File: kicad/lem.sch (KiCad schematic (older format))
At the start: 56 parts

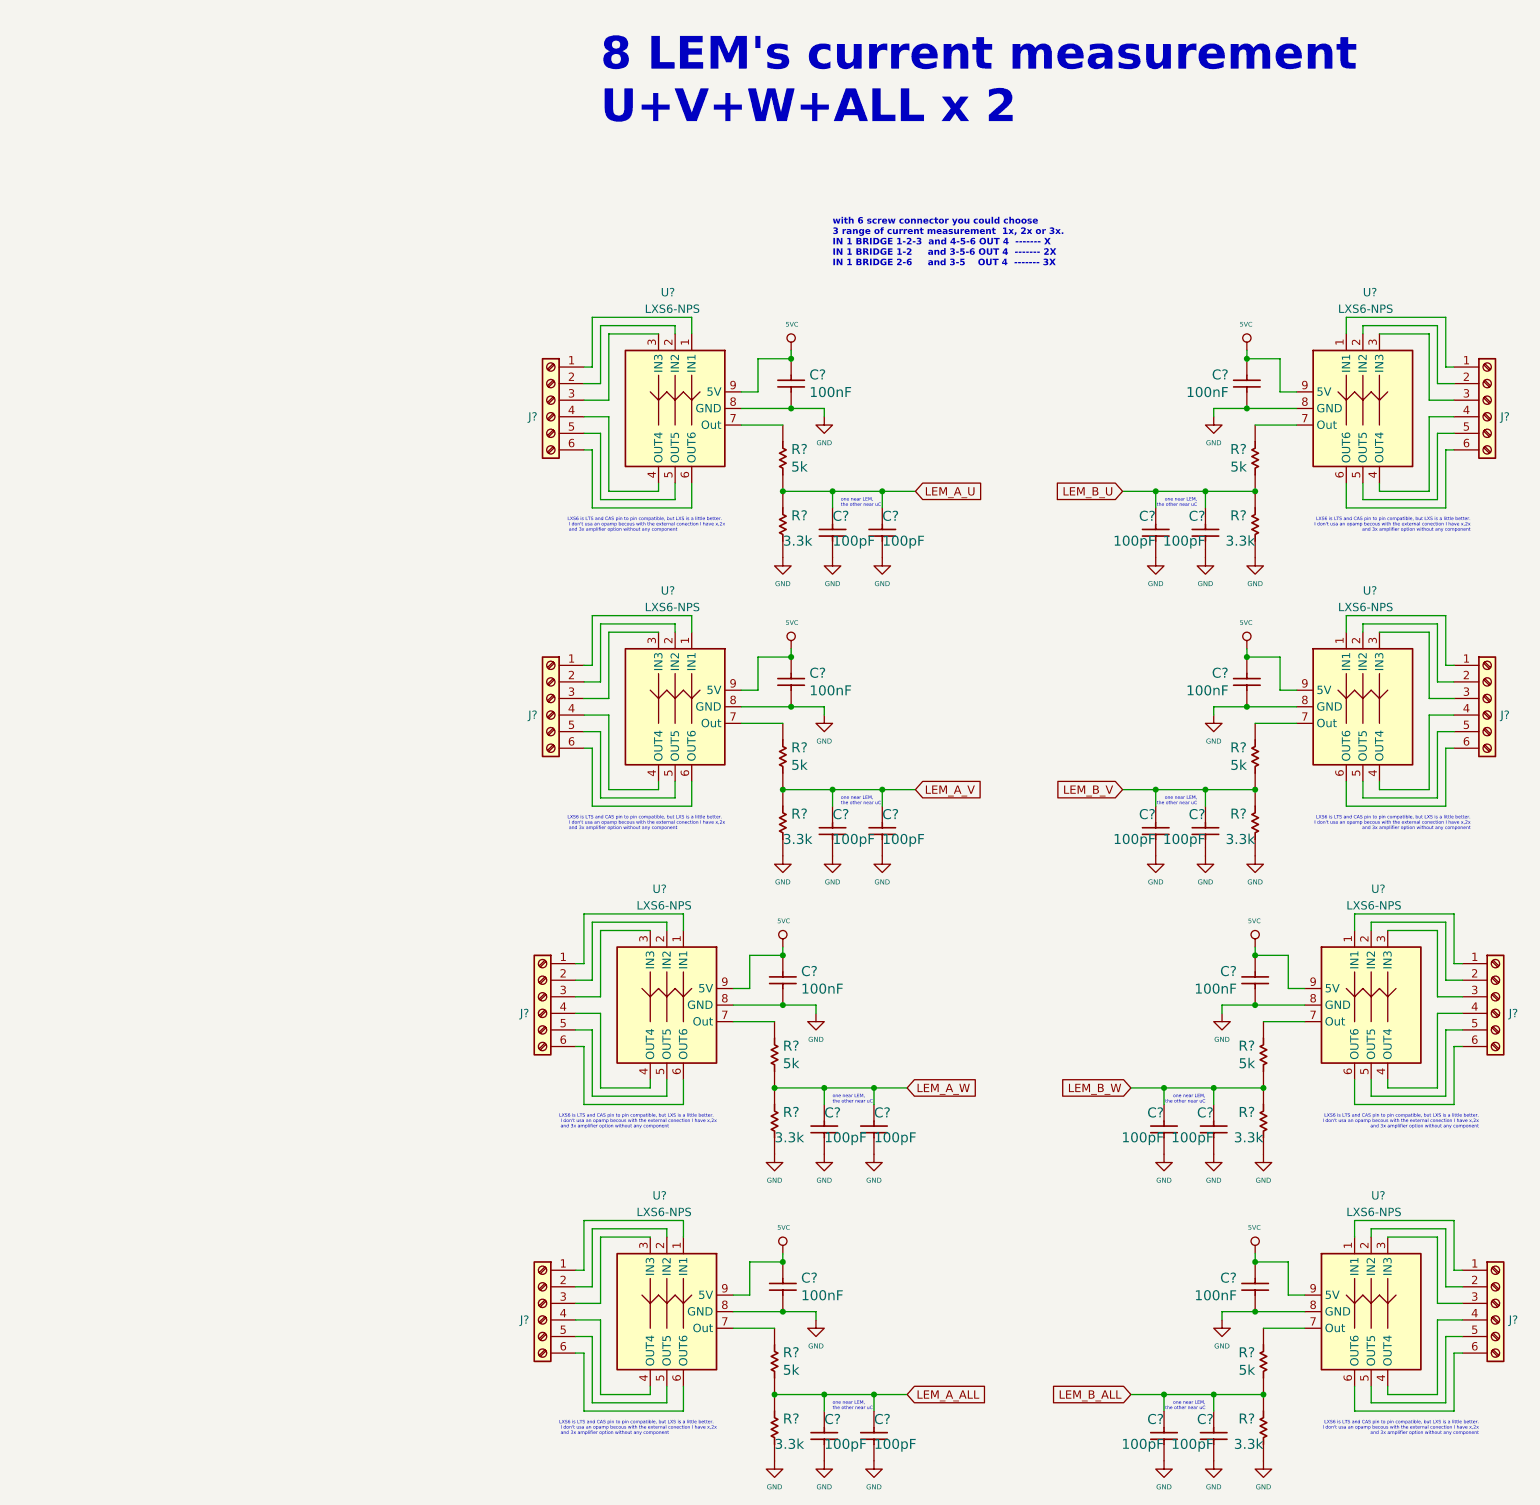
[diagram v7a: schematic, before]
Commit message: improve ethercat, embedded rj45 to spare, remove some unnecesary r's
I've worked on ethetcat/net to improve visibility on A3 page and also
remove some R's related to leds and change the embedded Rj45 for the
spare transformer and connector 'cause half the price and more options
to choose the connector shape and position
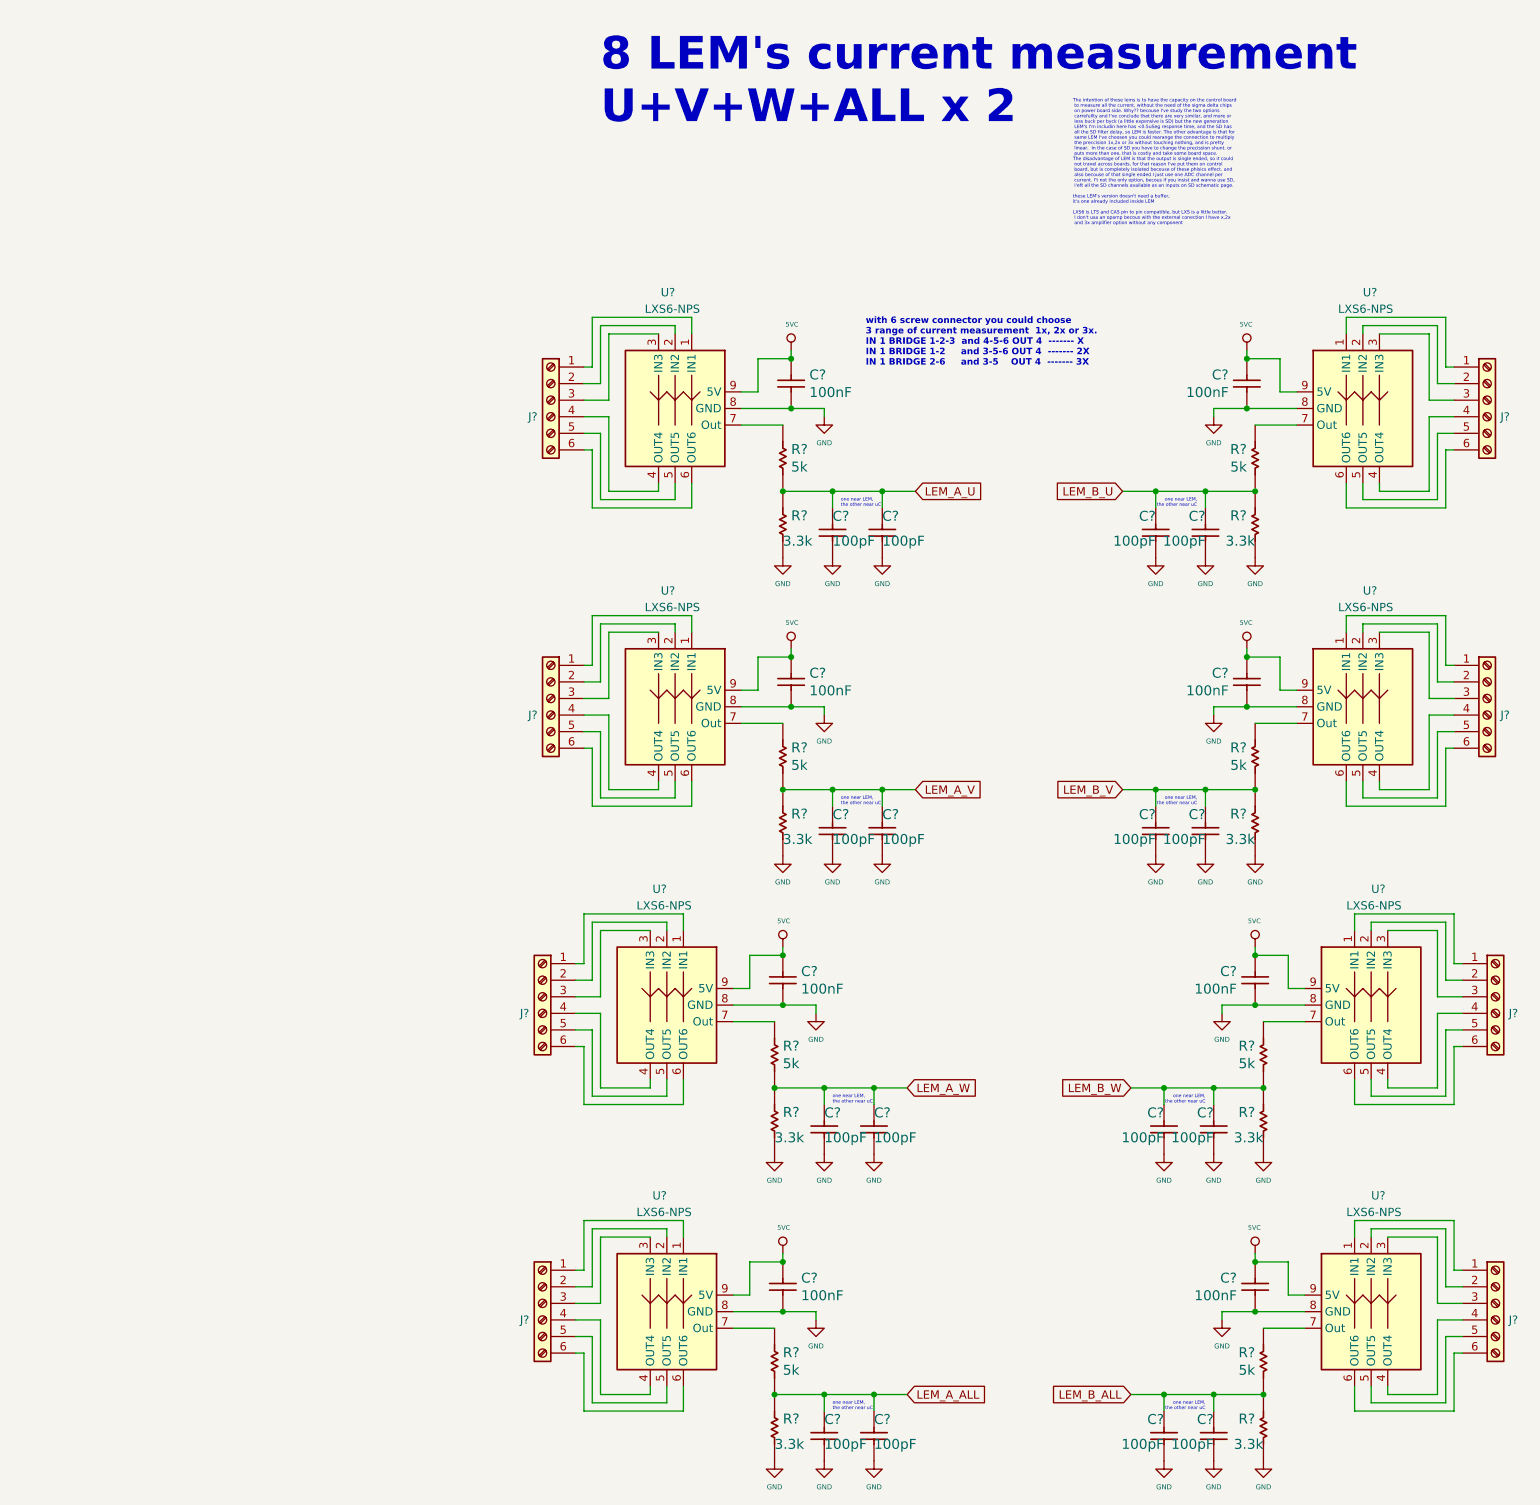
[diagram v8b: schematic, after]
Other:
- note added: "The intention of these lems is to have the capacity on the control board\n to measure all the current, without the need of the sigma delta chips\n on power board side. Why?? becouse I've study the two options\n carrefullty and I've conclude that there are very similar, and more or\n less buck per byck (a little expensive is SD) but the new generation\n LEM's I'm includin here has <0.5uSeg respons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"
- note removed: "LXS6 is LTS and CAS pin to pin compatible, but LXS is a little better.\n I don't usa an opamp becous with the external conection I have x,2x\n and 3x amplifier option without any component"
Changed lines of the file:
@@
 Wire Wire Line
 	5250 4700 5250 4650
-Text Notes 3900 5750 0    20   ~ 0
-LXS6 is LTS and CAS pin to pin compatible, but LXS is a little better.\n I don't usa an opamp becous with the external conection I have x,2x\n and 3x amplifier option without any component
-Text Notes 5500 2350 0    39   ~ 8
+Text Notes 5700 2950 0    39   ~ 8
 with 6 screw connector you could choose\n3 range of current measurement  1x, 2x or 3x.\nIN 1 BRIDGE 1-2-3  and 4-5-6 OUT 4  ------- X\nIN 1 BRIDGE 1-2     and 3-5-6 OUT 4  ------- 2X\nIN 1 BRIDGE 2-6     and 3-5    OUT 4  ------- 3X\n
 $Comp
@@
 Wire Wire Line
 	5250 2900 5250 2850
-Text Notes 3900 3950 0    20   ~ 0
-LXS6 is LTS and CAS pin to pin compatible, but LXS is a little better.\n I don't usa an opamp becous with the external conection I have x,2x\n and 3x amplifier option without any component
 $Comp
 L servo:Capacitor C?
@@
 Wire Wire Line
 	5200 6500 5200 6450
-Text Notes 3850 7550 0    20   ~ 0
-LXS6 is LTS and CAS pin to pin compatible, but LXS is a little better.\n I don't usa an opamp becous with the external conection I have x,2x\n and 3x amplifier option without any component
 $Comp
 L servo:Capacitor C?
@@
 Wire Wire Line
 	5200 8350 5200 8300
-Text Notes 3850 9400 0    20   ~ 0
-LXS6 is LTS and CAS pin to pin compatible, but LXS is a little better.\n I don't usa an opamp becous with the external conection I have x,2x\n and 3x amplifier option without any component
 $Comp
 L servo:Capacitor C?
@@
 Wire Wire Line
 	8000 4700 8000 4650
-Text Notes 9350 5750 2    20   ~ 0
-LXS6 is LTS and CAS pin to pin compatible, but LXS is a little better.\n I don't usa an opamp becous with the external conection I have x,2x\n and 3x amplifier option without any component
 $Comp
 L servo:Capacitor C?
@@
 Wire Wire Line
 	8000 2900 8000 2850
-Text Notes 9350 3950 2    20   ~ 0
-LXS6 is LTS and CAS pin to pin compatible, but LXS is a little better.\n I don't usa an opamp becous with the external conection I have x,2x\n and 3x amplifier option without any component
 $Comp
 L servo:Capacitor C?
@@
 Wire Wire Line
 	8050 6500 8050 6450
-Text Notes 9400 7550 2    20   ~ 0
-LXS6 is LTS and CAS pin to pin compatible, but LXS is a little better.\n I don't usa an opamp becous with the external conection I have x,2x\n and 3x amplifier option without any component
 $Comp
 L servo:Capacitor C?
@@
 Wire Wire Line
 	8050 8350 8050 8300
-Text Notes 9400 9400 2    20   ~ 0
-LXS6 is LTS and CAS pin to pin compatible, but LXS is a little better.\n I don't usa an opamp becous with the external conection I have x,2x\n and 3x amplifier option without any component
 $Comp
 L servo:Capacitor C?
@@
 Text Notes 4100 1500 0    197  ~ 39
 8 LEM's current measurement \nU+V+W+ALL x 2
+Text Notes 6950 2100 0    20   ~ 0
+The intention of these lems is to have the capacity on the control board\n to measure all the current, without the need of the sigma delta chips\n on power board side. Why?? becouse I've study the two options\n carrefullty and I've conclude that there are very similar, and more or\n less buck per byck (a little expensive is SD) but the new generation\n LEM's I'm includin here has <0.5uSeg response time, and the SD has\n all the SD filter delay, so LEM is faster. The other advantage is that for\n same LEM I've choosen you could rearange the connection to multiply\n the preccision 1x,2x or 3x without touching nothing, and is pretty\n linear.  In the case of SD you have to change the precission shunt. or\n puts more than one, that is costly and take some board space.\nThe disadvantage of LEM is that the output is single ended, so it could\n not travel across boards, for that reason I've put them on control\n board, but is completely isolated becouse of these phisics effect. and\n also becouse of that single ended I just use one ADC channel per\n current. I't not the only option, becous if you insist and wanna use SD,\n I'eft all the SD channels available as an inputs on SD schematic page.\n\nthese LEM's version doesn't need a buffer, \nit's one already included inside LEM\n\nLXS6 is LTS and CAS pin to pin compatible, but LXS is a little better.\n I don't usa an opamp becous with the external conection I have x,2x\n and 3x amplifier option without any component\n
 $EndSCHEMATC
